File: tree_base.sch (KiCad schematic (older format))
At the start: 16 parts, among them Q1 DMG2302U, SW1 SW_SPDT, U1 MCP1640BCH

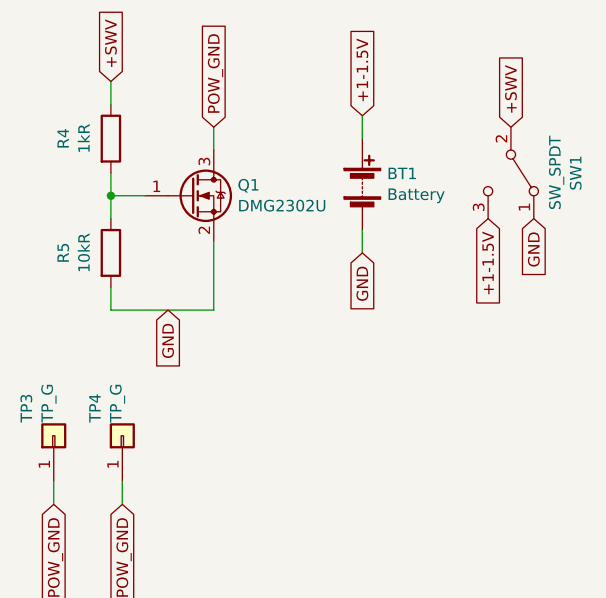
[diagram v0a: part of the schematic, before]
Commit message: Update with changes to use attiny13a only
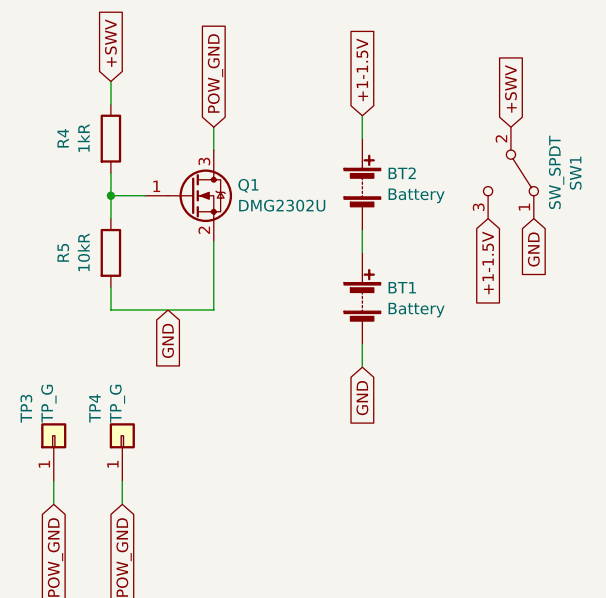
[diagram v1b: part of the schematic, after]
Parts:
- added BT2: Battery, Battery:BatteryHolder_Keystone_2466_1xAAA, symbol Device:Battery
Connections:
- net +1-1.5V: now also BT2.1 (+); no longer BT1.1 (+)
- new net: BT1.1 (+), BT2.2 (-)
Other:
- moved on the sheet: BT1
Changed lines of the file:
@@
 L Device:Battery BT1
 U 1 1 5FBBBC4B
-P 7800 3650
-F 0 "BT1" H 7908 3696 50  0000 L CNN
-F 1 "Battery" H 7908 3605 50  0000 L CNN
-F 2 "Battery:BatteryHolder_Keystone_2466_1xAAA" V 7800 3710 50  0001 C CNN
-F 3 "~" V 7800 3710 50  0001 C CNN
-	1    7800 3650
+P 7800 4150
+F 0 "BT1" H 7908 4196 50  0000 L CNN
+F 1 "Battery" H 7908 4105 50  0000 L CNN
+F 2 "Battery:BatteryHolder_Keystone_2466_1xAAA" V 7800 4210 50  0001 C CNN
+F 3 "~" V 7800 4210 50  0001 C CNN
+	1    7800 4150
 	1    0    0    -1
 $EndComp
 Text GLabel 7800 3350 1    50   Input ~ 0
 +1-1.5V
-Text GLabel 7800 3950 3    50   Input ~ 0
+Text GLabel 7800 4450 3    50   Input ~ 0
 GND
 Wire Wire Line
 	7800 3350 7800 3450
 Wire Wire Line
-	7800 3850 7800 3950
+	7800 4350 7800 4450
 Text GLabel 8450 3400 1    50   Input ~ 0
 +SWV
@@
 	0    -1   -1   0
 $EndComp
+$Comp
+L Device:Battery BT2
+U 1 1 5FCFDB04
+P 7800 3650
+F 0 "BT2" H 7908 3696 50  0000 L CNN
+F 1 "Battery" H 7908 3605 50  0000 L CNN
+F 2 "Battery:BatteryHolder_Keystone_2466_1xAAA" V 7800 3710 50  0001 C CNN
+F 3 "~" V 7800 3710 50  0001 C CNN
+	1    7800 3650
+	1    0    0    -1
+$EndComp
+Wire Wire Line
+	7800 3950 7800 3850
 $EndSCHEMATC

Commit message: Add USB variant; update to use 3xAAA
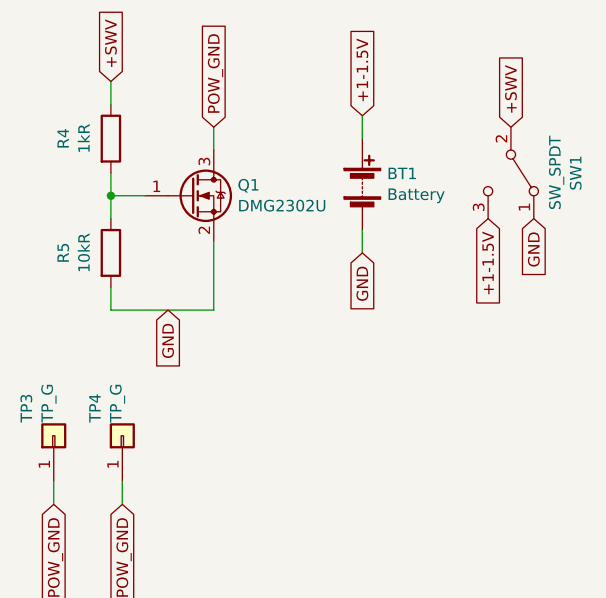
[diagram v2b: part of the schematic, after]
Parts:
- removed BT2: Battery, Battery:BatteryHolder_Keystone_2466_1xAAA, symbol Device:Battery
- BT1: footprint Battery:BatteryHolder_Keystone_2466_1xAAA -> Battery:BatteryHolder_Keystone_2479_3xAAA
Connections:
- net +1-1.5V: now also BT1.1 (+)
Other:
- moved on the sheet: BT1
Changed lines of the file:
@@
 L Device:Battery BT1
 U 1 1 5FBBBC4B
-P 7800 4150
-F 0 "BT1" H 7908 4196 50  0000 L CNN
-F 1 "Battery" H 7908 4105 50  0000 L CNN
-F 2 "Battery:BatteryHolder_Keystone_2466_1xAAA" V 7800 4210 50  0001 C CNN
-F 3 "~" V 7800 4210 50  0001 C CNN
-	1    7800 4150
+P 7800 3650
+F 0 "BT1" H 7908 3696 50  0000 L CNN
+F 1 "Battery" H 7908 3605 50  0000 L CNN
+F 2 "Battery:BatteryHolder_Keystone_2479_3xAAA" V 7800 3710 50  0001 C CNN
+F 3 "~" V 7800 3710 50  0001 C CNN
+	1    7800 3650
 	1    0    0    -1
 $EndComp
 Text GLabel 7800 3350 1    50   Input ~ 0
 +1-1.5V
-Text GLabel 7800 4450 3    50   Input ~ 0
+Text GLabel 7800 3950 3    50   Input ~ 0
 GND
 Wire Wire Line
 	7800 3350 7800 3450
 Wire Wire Line
-	7800 4350 7800 4450
+	7800 3850 7800 3950
 Text GLabel 8450 3400 1    50   Input ~ 0
 +SWV
@@
 	0    -1   -1   0
 $EndComp
-$Comp
-L Device:Battery BT2
-U 1 1 5FCFDB04
-P 7800 3650
-F 0 "BT2" H 7908 3696 50  0000 L CNN
-F 1 "Battery" H 7908 3605 50  0000 L CNN
-F 2 "Battery:BatteryHolder_Keystone_2466_1xAAA" V 7800 3710 50  0001 C CNN
-F 3 "~" V 7800 3710 50  0001 C CNN
-	1    7800 3650
-	1    0    0    -1
-$EndComp
-Wire Wire Line
-	7800 3950 7800 3850
 $EndSCHEMATC
